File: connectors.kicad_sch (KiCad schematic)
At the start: 3 parts

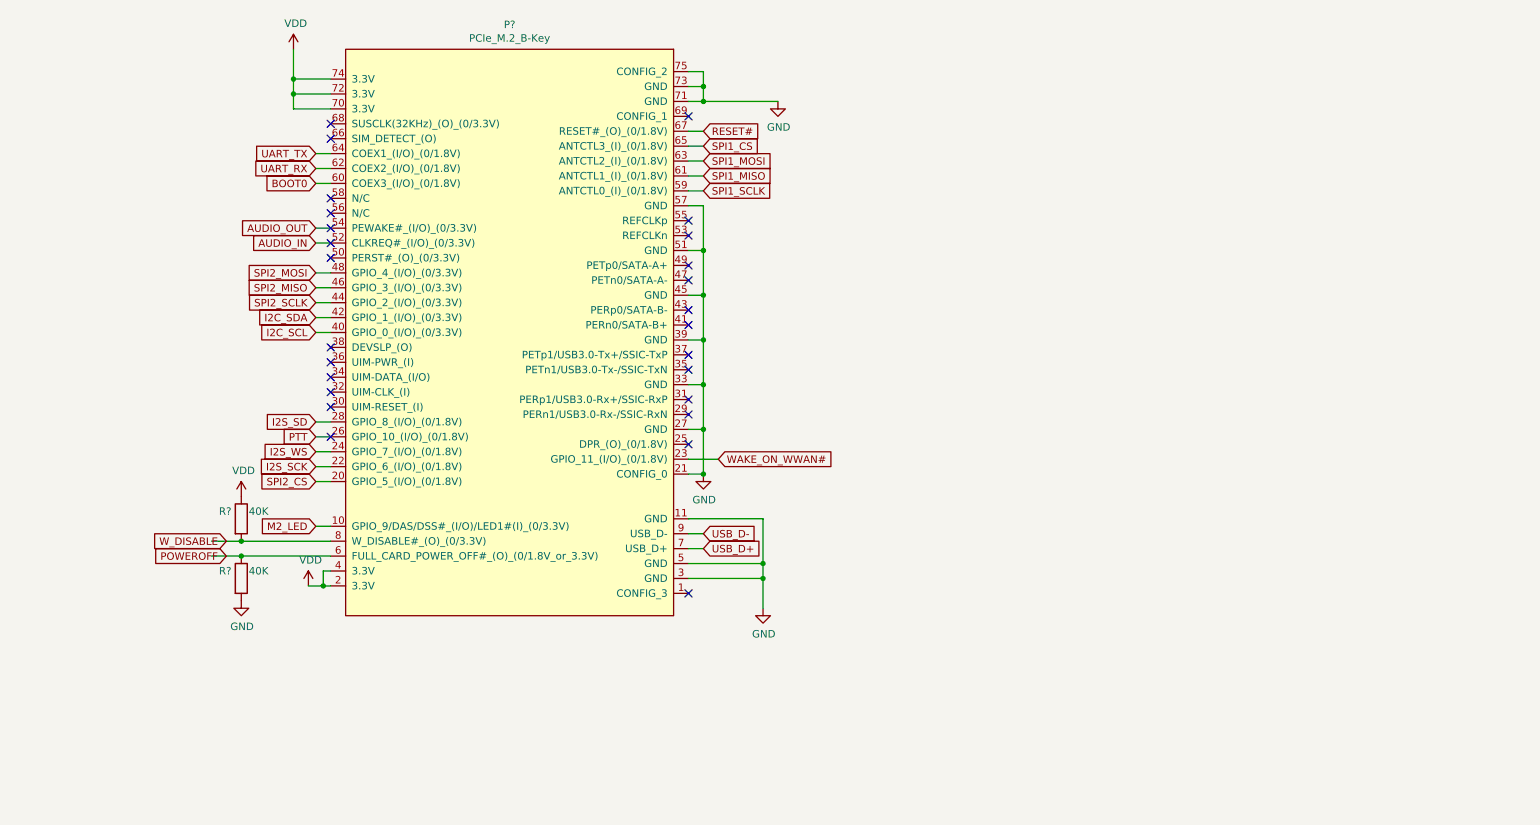
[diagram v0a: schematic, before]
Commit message: Changed MCU and M.2 pin assignment
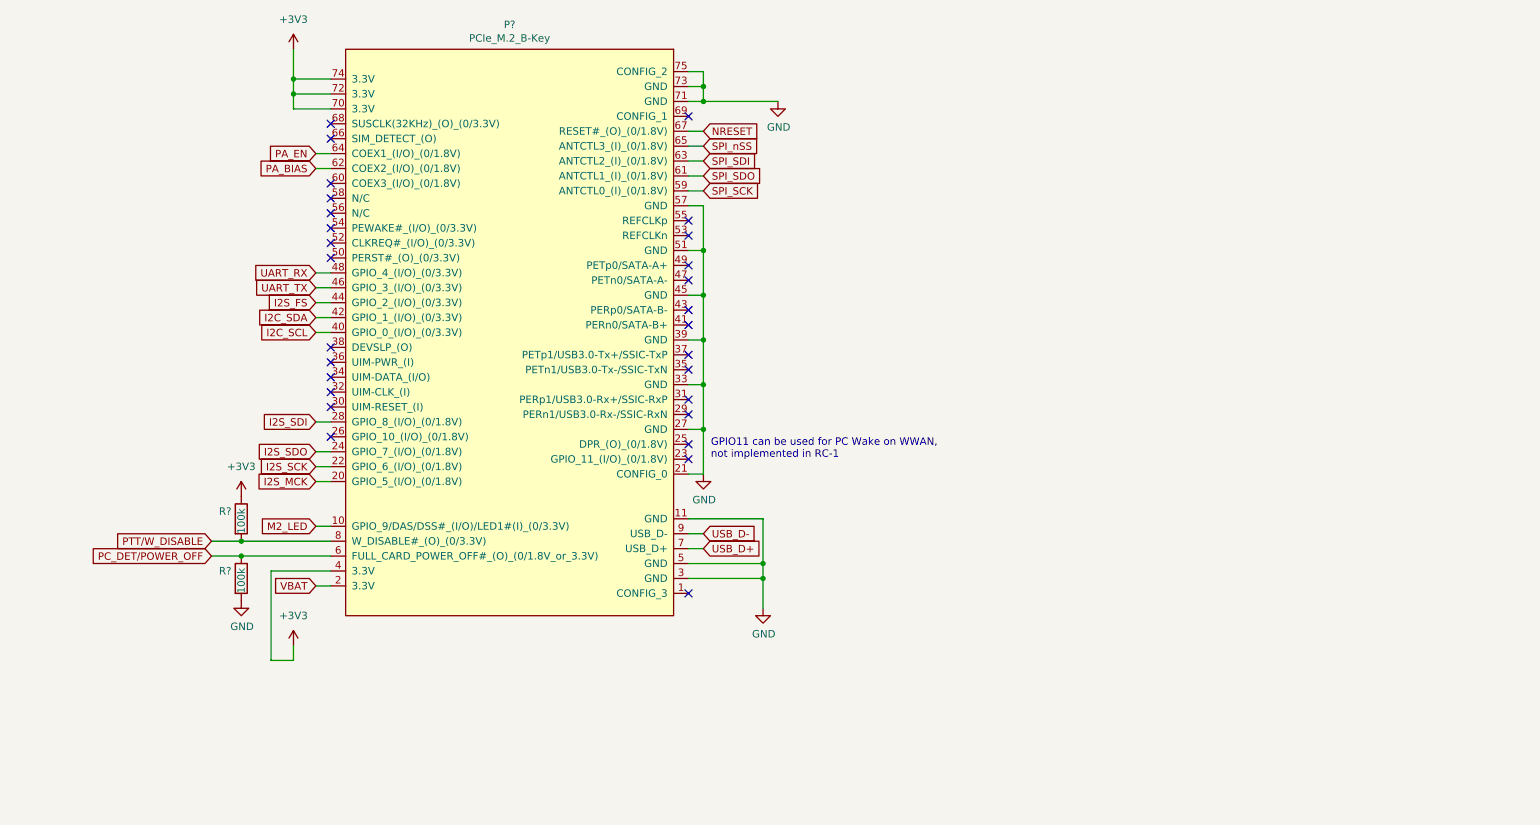
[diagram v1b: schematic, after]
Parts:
- R? (x2): value 40K -> 100k
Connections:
- net SPI2_MISO is gone; now on net UART_TX: P?.46 (GPIO_3_(I/O)_(0/3.3V))
- net SPI2_MOSI is gone; now on net UART_RX: P?.48 (GPIO_4_(I/O)_(0/3.3V))
- net UART_RX: no longer P?.62 (COEX2_(I/O)_(0/1.8V))
- net UART_TX: no longer P?.64 (COEX1_(I/O)_(0/1.8V))
- net AUDIO_IN: no longer names the net of P?.52 (CLKREQ#_(I/O)_(0/3.3V))
- net AUDIO_OUT: no longer names the net of P?.54 (PEWAKE#_(I/O)_(0/3.3V))
- net BOOT0: no longer names the net of P?.60 (COEX3_(I/O)_(0/1.8V))
- net I2S_SD renamed I2S_SDI
- net I2S_WS renamed I2S_SDO
- net POWEROFF renamed PC_DET/POWER_OFF
- net PTT: no longer names the net of P?.26 (GPIO_10_(I/O)_(0/1.8V))
- net RESET# renamed NRESET
- net SPI1_CS renamed SPI_nSS
- net SPI1_MISO renamed SPI_SDO
- net SPI1_MOSI renamed SPI_SDI
- net SPI1_SCLK renamed SPI_SCK
- net SPI2_CS renamed I2S_MCK
- net SPI2_SCLK renamed I2S_FS
- net VDD renamed +3V3
- net +3V3: no longer P?.2 (3.3V)
- net WAKE_ON_WWAN#: no longer names the net of P?.23 (GPIO_11_(I/O)_(0/1.8V))
- net W_DISABLE renamed PTT/W_DISABLE
- new net PA_BIAS: P?.62 (COEX2_(I/O)_(0/1.8V))
- new net PA_EN: P?.64 (COEX1_(I/O)_(0/1.8V))
- new net VBAT: P?.2 (3.3V)
- no-connect marks 26 -> 28
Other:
- note added: "GPIO11 can be used for PC Wake on WWAN, not implemented in RC-1"

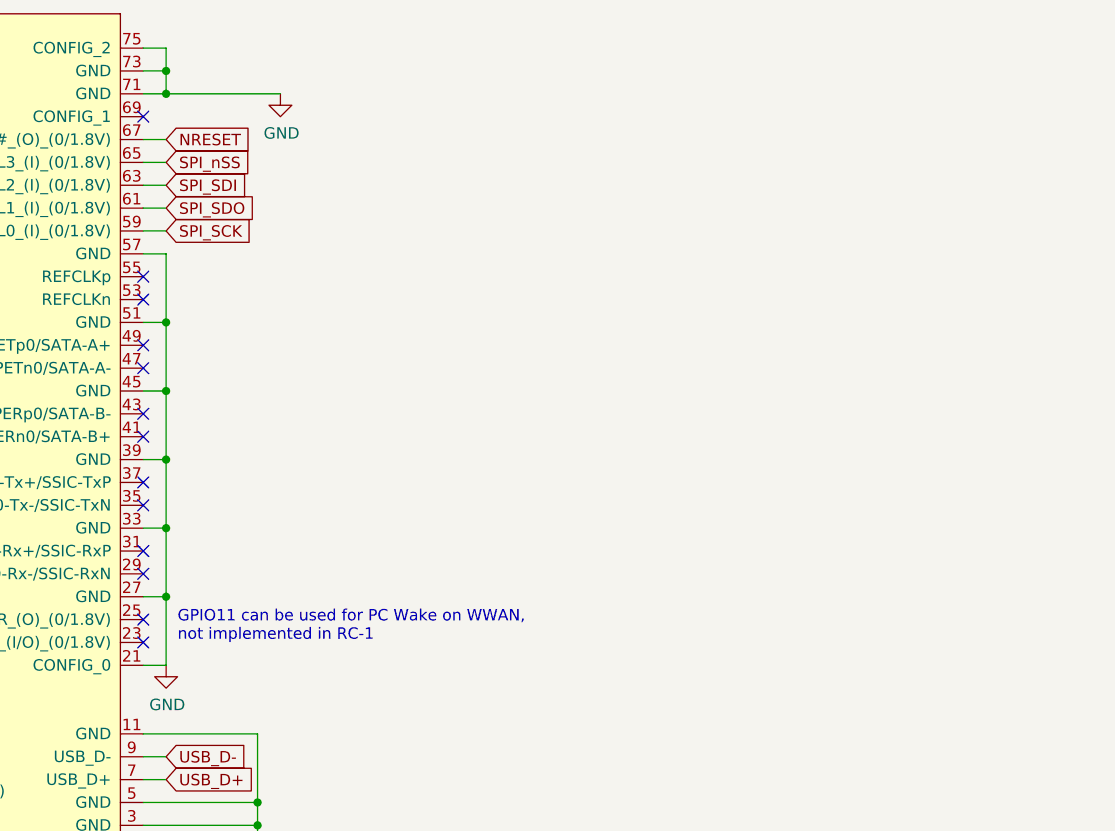
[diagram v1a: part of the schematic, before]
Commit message: Add SOICbite SWD+UART connector
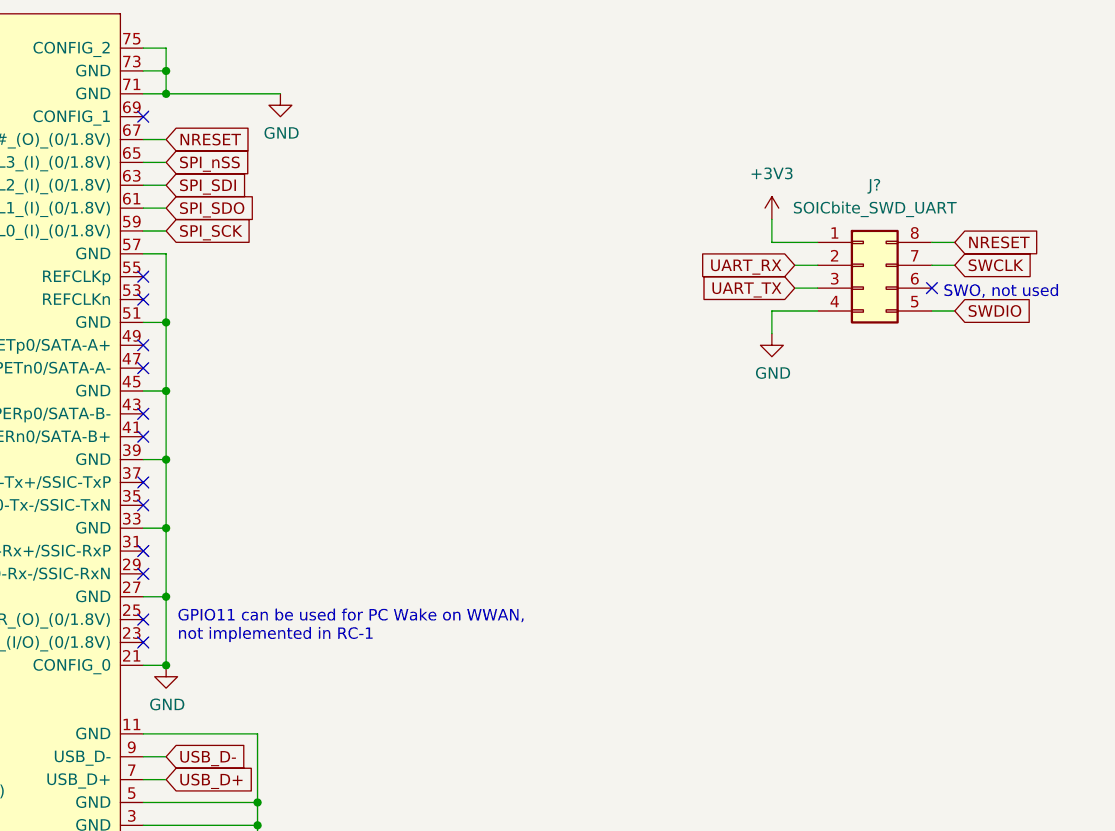
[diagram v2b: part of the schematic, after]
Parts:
- added J?: SOICbite_SWD_UART, SOICbite:SOIC_clipProgSmall, symbol Connector_Generic:Conn_02x04_Counter_Clockwise
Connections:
- net +3V3: now also J?.1 (Pin_1)
- net GND: now also J?.4 (Pin_4)
- net NRESET: now also J?.8 (Pin_8)
- net UART_RX: now also J?.2 (Pin_2)
- net UART_TX: now also J?.3 (Pin_3)
- new net SWCLK: J?.7 (Pin_7)
- new net SWDIO: J?.5 (Pin_5)
- no-connect marks 28 -> 29
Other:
- note added: "SWO, not used"
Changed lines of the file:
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@@
   (junction (at 148.59 130.81) (diameter 0) (color 0 0 0 0)
   )
+  (junction (at 138.43 113.03) (diameter 0) (color 0 0 0 0)
+  )
   (junction (at 59.69 127) (diameter 0) (color 0 0 0 0)
   )
+  (no_connect (at 223.52 71.12))
   (no_connect (at 135.89 92.71))
   (no_connect (at 74.93 55.88))
@@
   (no_connect (at 135.89 80.01))
   (no_connect (at 135.89 102.87))
+  (wire (pts (xy 210.82 66.04) (xy 205.74 66.04))
+    (stroke (width 0) (type default) (color 0 0 0 0))
+  )
   (wire (pts (xy 138.43 97.79) (xy 138.43 105.41))
     (stroke (width 0) (type default) (color 0 0 0 0))
@@
     (stroke (width 0) (type default) (color 0 0 0 0))
   )
+  (wire (pts (xy 208.28 68.58) (xy 210.82 68.58))
+    (stroke (width 0) (type default) (color 0 0 0 0))
+  )
   (wire (pts (xy 148.59 120.65) (xy 148.59 128.27))
     (stroke (width 0) (type default) (color 0 0 0 0))
@@
     (stroke (width 0) (type default) (color 0 0 0 0))
   )
+  (wire (pts (xy 223.52 73.66) (xy 226.06 73.66))
+    (stroke (width 0) (type default) (color 0 0 0 0))
+  )
   (wire (pts (xy 72.39 60.96) (xy 74.93 60.96))
     (stroke (width 0) (type default) (color 0 0 0 0))
@@
     (stroke (width 0) (type default) (color 0 0 0 0))
   )
+  (wire (pts (xy 205.74 73.66) (xy 210.82 73.66))
+    (stroke (width 0) (type default) (color 0 0 0 0))
+  )
   (wire (pts (xy 54.61 124.46) (xy 59.69 124.46))
     (stroke (width 0) (type default) (color 0 0 0 0))
@@
     (stroke (width 0) (type default) (color 0 0 0 0))
   )
+  (wire (pts (xy 223.52 68.58) (xy 226.06 68.58))
+    (stroke (width 0) (type default) (color 0 0 0 0))
+  )
   (wire (pts (xy 135.89 74.93) (xy 138.43 74.93))
     (stroke (width 0) (type default) (color 0 0 0 0))
@@
     (stroke (width 0) (type default) (color 0 0 0 0))
   )
+  (wire (pts (xy 208.28 71.12) (xy 210.82 71.12))
+    (stroke (width 0) (type default) (color 0 0 0 0))
+  )
   (wire (pts (xy 138.43 46.99) (xy 138.43 49.53))
     (stroke (width 0) (type default) (color 0 0 0 0))
@@
     (stroke (width 0) (type default) (color 0 0 0 0))
   )
+  (wire (pts (xy 205.74 66.04) (xy 205.74 63.5))
+    (stroke (width 0) (type default) (color 0 0 0 0))
+  )
   (wire (pts (xy 135.89 62.23) (xy 138.43 62.23))
     (stroke (width 0) (type default) (color 0 0 0 0))
@@
     (stroke (width 0) (type default) (color 0 0 0 0))
   )
+  (wire (pts (xy 223.52 66.04) (xy 226.06 66.04))
+    (stroke (width 0) (type default) (color 0 0 0 0))
+  )
   (wire (pts (xy 135.89 44.45) (xy 138.43 44.45))
     (stroke (width 0) (type default) (color 0 0 0 0))
@@
   (wire (pts (xy 135.89 125.73) (xy 138.43 125.73))
     (stroke (width 0) (type default) (color 0 0 0 0))
+  )
+  (wire (pts (xy 205.74 76.2) (xy 205.74 73.66))
+    (stroke (width 0) (type default) (color 0 0 0 0))
+  )
+  (text "SWO, not used" (at 224.79 72.39 0)
+    (effects (font (size 1.27 1.27)) (justify left bottom))
   )
   (text "GPIO11 can be used for PC Wake on WWAN, \nnot implemented in RC-1"
@@
     )
   )
+  (global_label "UART_TX" (shape input) (at 208.28 71.12 180) (fields_autoplaced)
+    (effects (font (size 1.27 1.27)) (justify right))
+    (property "Intersheet References" "${INTERSHEET_REFS}" (id 0) (at 198.1544 71.0406 0)
+      (effects (font (size 1.27 1.27)) (justify right) hide)
+    )
+  )
   (global_label "M2_LED" (shape input) (at 72.39 121.92 180) (fields_autoplaced)
     (effects (font (size 1.27 1.27)) (justify right))
@@
     )
   )
+  (global_label "UART_RX" (shape input) (at 208.28 68.58 180) (fields_autoplaced)
+    (effects (font (size 1.27 1.27)) (justify right))
+    (property "Intersheet References" "${INTERSHEET_REFS}" (id 0) (at 197.852 68.5006 0)
+      (effects (font (size 1.27 1.27)) (justify right) hide)
+    )
+  )
   (global_label "PA_EN" (shape input) (at 72.39 58.42 180) (fields_autoplaced)
     (effects (font (size 1.27 1.27)) (justify right))
@@
     )
   )
+  (global_label "SWCLK" (shape input) (at 226.06 68.58 0) (fields_autoplaced)
+    (effects (font (size 1.27 1.27)) (justify left))
+    (property "Intersheet References" "${INTERSHEET_REFS}" (id 0) (at 234.6132 68.6594 0)
+      (effects (font (size 1.27 1.27)) (justify left) hide)
+    )
+  )
   (global_label "UART_TX" (shape input) (at 72.39 81.28 180) (fields_autoplaced)
     (effects (font (size 1.27 1.27)) (justify right))
@@
     )
   )
+  (global_label "SWDIO" (shape input) (at 226.06 73.66 0) (fields_autoplaced)
+    (effects (font (size 1.27 1.27)) (justify left))
+    (property "Intersheet References" "${INTERSHEET_REFS}" (id 0) (at 234.2504 73.7394 0)
+      (effects (font (size 1.27 1.27)) (justify left) hide)
+    )
+  )
   (global_label "I2S_MCK" (shape input) (at 72.39 114.3 180) (fields_autoplaced)
     (effects (font (size 1.27 1.27)) (justify right))
@@
     (property "Intersheet References" "${INTERSHEET_REFS}" (id 0) (at 62.9901 104.2194 0)
       (effects (font (size 1.27 1.27)) (justify right) hide)
+    )
+  )
+  (global_label "NRESET" (shape input) (at 226.06 66.04 0) (fields_autoplaced)
+    (effects (font (size 1.27 1.27)) (justify left))
+    (property "Intersheet References" "${INTERSHEET_REFS}" (id 0) (at 235.4599 66.1194 0)
+      (effects (font (size 1.27 1.27)) (justify left) hide)
     )
   )
@@
     (pin "1")
     (pin "2")
+  )
+  (symbol (lib_id "Connector_Generic:Conn_02x04_Counter_Clockwise") (at 215.9 68.58 0) (unit 1)
+    (in_bom yes) (on_board yes) (fields_autoplaced)
+    (property "Reference" "J?" (id 0) (at 217.17 59.69 0))
+    (property "Value" "SOICbite_SWD_UART" (id 1) (at 217.17 62.23 0))
+    (property "Footprint" "SOICbite:SOIC_clipProgSmall" (id 2) (at 215.9 68.58 0)
+      (effects (font (size 1.27 1.27)) hide)
+    )
+    (property "Datasheet" "https://github.com/SimonMerrett/SOICbite/blob/master/README.md" (id 3) (at 215.9 68.58 0)
+      (effects (font (size 1.27 1.27)) hide)
+    )
+    (pin "1")
+    (pin "2")
+    (pin "3")
+    (pin "4")
+    (pin "5")
+    (pin "6")
+    (pin "7")
+    (pin "8")
   )
   (symbol (lib_id "Device:R") (at 59.69 130.81 0) (unit 1)
@@
     (pin "1")
   )
+  (symbol (lib_id "power:+3V3") (at 205.74 63.5 0) (unit 1)
+    (in_bom yes) (on_board yes) (fields_autoplaced)
+    (property "Reference" "#PWR?" (id 0) (at 205.74 67.31 0)
+      (effects (font (size 1.27 1.27)) hide)
+    )
+    (property "Value" "+3V3" (id 1) (at 205.74 58.42 0))
+    (property "Footprint" "" (id 2) (at 205.74 63.5 0)
+      (effects (font (size 1.27 1.27)) hide)
+    )
+    (property "Datasheet" "" (id 3) (at 205.74 63.5 0)
+      (effects (font (size 1.27 1.27)) hide)
+    )
+    (pin "1")
+  )
   (symbol (lib_id "power:+3V3") (at 59.69 116.84 0) (unit 1)
     (in_bom yes) (on_board yes) (fields_autoplaced)
@@
       (effects (font (size 1.27 1.27)) hide)
     )
+    (pin "1")
+  )
+  (symbol (lib_id "power:GND") (at 205.74 76.2 0) (unit 1)
+    (in_bom yes) (on_board yes)
+    (property "Reference" "#PWR?" (id 0) (at 205.74 82.55 0)
+      (effects (font (size 1.27 1.27)) hide)
+    )
+    (property "Value" "GND" (id 1) (at 205.867 80.5942 0))
+    (property "Footprint" "" (id 2) (at 205.74 76.2 0)
+      (effects (font (size 1.27 1.27)) hide)
+    )
+    (property "Datasheet" "" (id 3) (at 205.74 76.2 0)
+      (effects (font (size 1.27 1.27)) hide)
+    )
